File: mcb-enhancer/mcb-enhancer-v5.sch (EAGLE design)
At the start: 127 parts, among them T1 BT138-F, T2 BT138-F, T3 BT138-F, T4 BT138-F, T5 BT138-F, T6 BT138-F, T7 BT138-F, T8 BT138-F

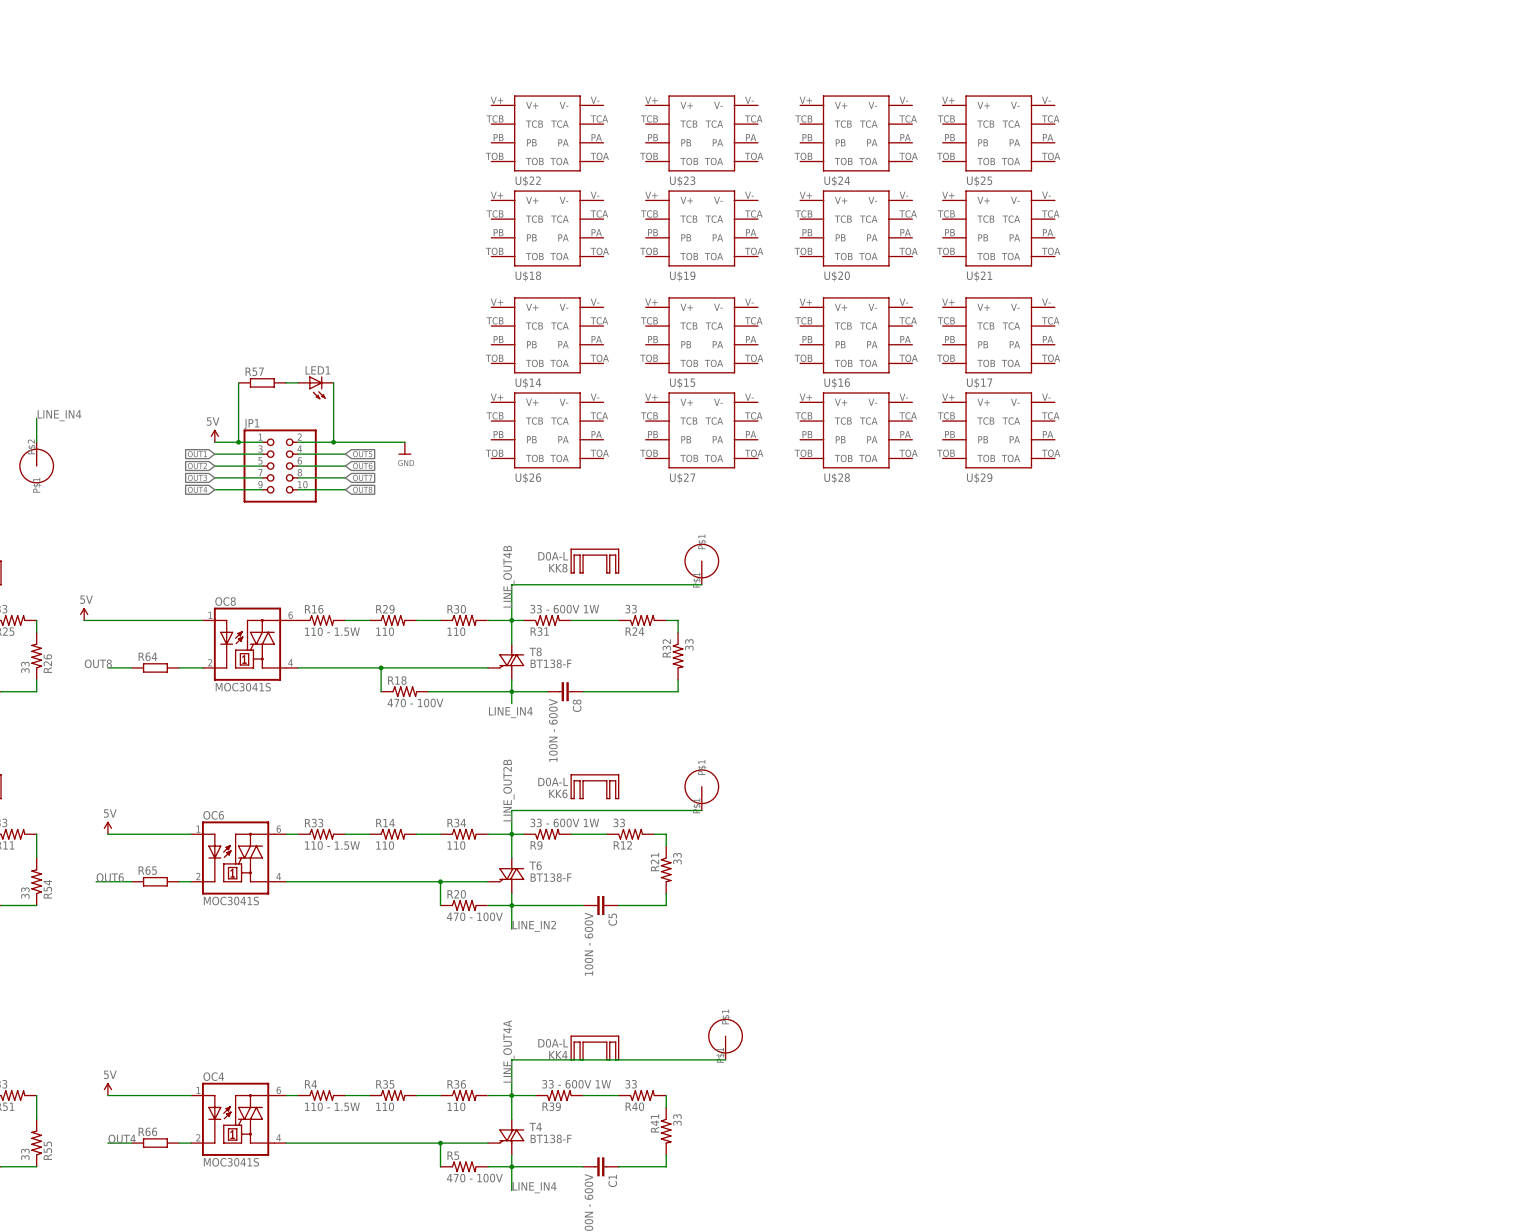
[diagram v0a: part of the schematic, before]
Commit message: add mcb enhancer BoM and gerber
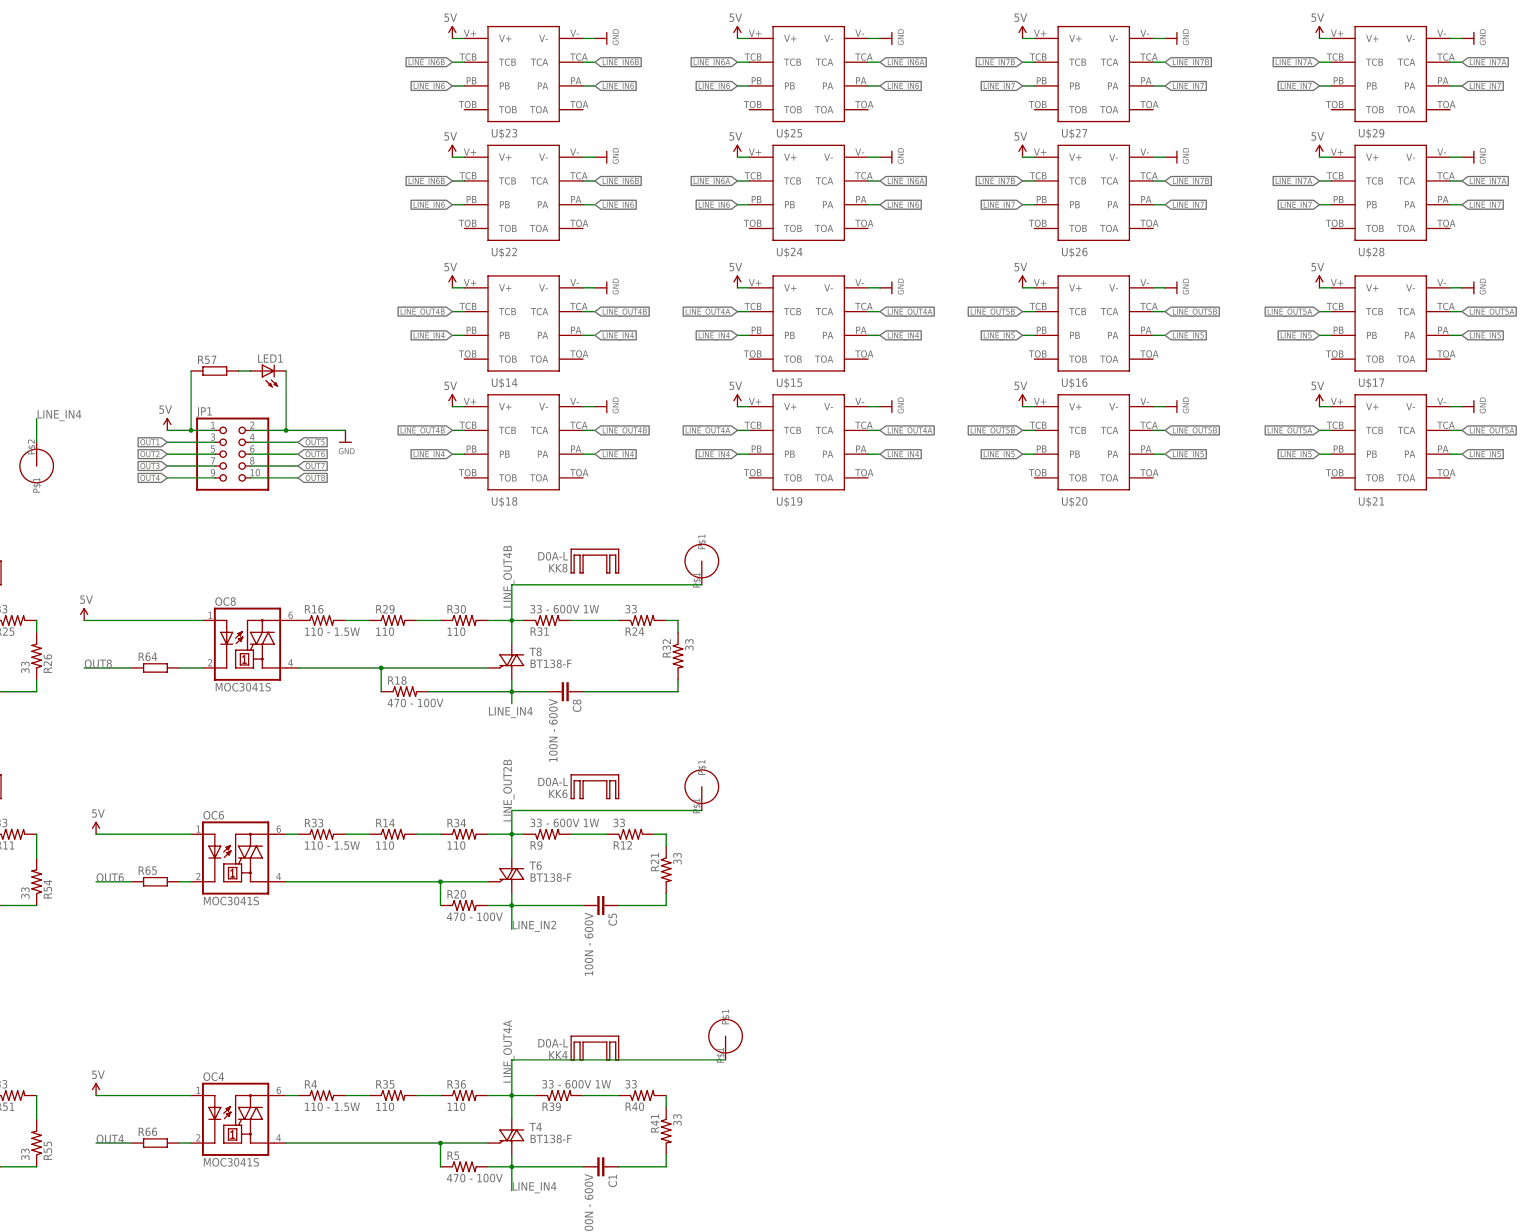
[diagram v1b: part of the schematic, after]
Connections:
- new net LINE_IN5: U$16.PA, U$16.PB, U$17.PA, U$17.PB, U$20.PA, U$20.PB, U$21.PA, U$21.PB
- new net LINE_IN6: U$22.PA, U$22.PB, U$23.PA, U$23.PB, U$24.PA, U$24.PB, U$25.PA, U$25.PB
- new net LINE_IN6A: U$24.TCA, U$24.TCB, U$25.TCA, U$25.TCB
- new net LINE_IN6B: U$22.TCA, U$22.TCB, U$23.TCA, U$23.TCB
- new net LINE_IN7: U$26.PA, U$26.PB, U$27.PA, U$27.PB, U$28.PA, U$28.PB, U$29.PA, U$29.PB
- new net LINE_IN7A: U$28.TCA, U$28.TCB, U$29.TCA, U$29.TCB
- new net LINE_IN7B: U$26.TCA, U$26.TCB, U$27.TCA, U$27.TCB
- new net LINE_OUT5A: U$17.TCA, U$17.TCB, U$21.TCA, U$21.TCB
- new net LINE_OUT5B: U$16.TCA, U$16.TCB, U$20.TCA, U$20.TCB
- net 5V: now also U$14.V+, U$15.V+, U$16.V+, U$17.V+, U$18.V+, U$19.V+, U$20.V+, U$21.V+, U$22.V+, U$23.V+, U$24.V+, U$25.V+, U$26.V+, U$27.V+, U$28.V+, U$29.V+
- net GND: now also U$14.V-, U$15.V-, U$16.V-, U$17.V-, U$18.V-, U$19.V-, U$20.V-, U$21.V-, U$22.V-, U$23.V-, U$24.V-, U$25.V-, U$26.V-, U$27.V-, U$28.V-, U$29.V-
- net LINE_IN4: now also U$14.PA, U$14.PB, U$15.PA, U$15.PB, U$18.PA, U$18.PB, U$19.PA, U$19.PB
- net LINE_OUT4A: now also U$15.TCA, U$15.TCB, U$19.TCA, U$19.TCB
- net LINE_OUT4B: now also U$14.TCA, U$14.TCB, U$18.TCA, U$18.TCB
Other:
- moved on the sheet: JP1, LED1, R57, U$14, U$15, U$16, U$17, U$18, U$19, U$20, U$21, U$22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

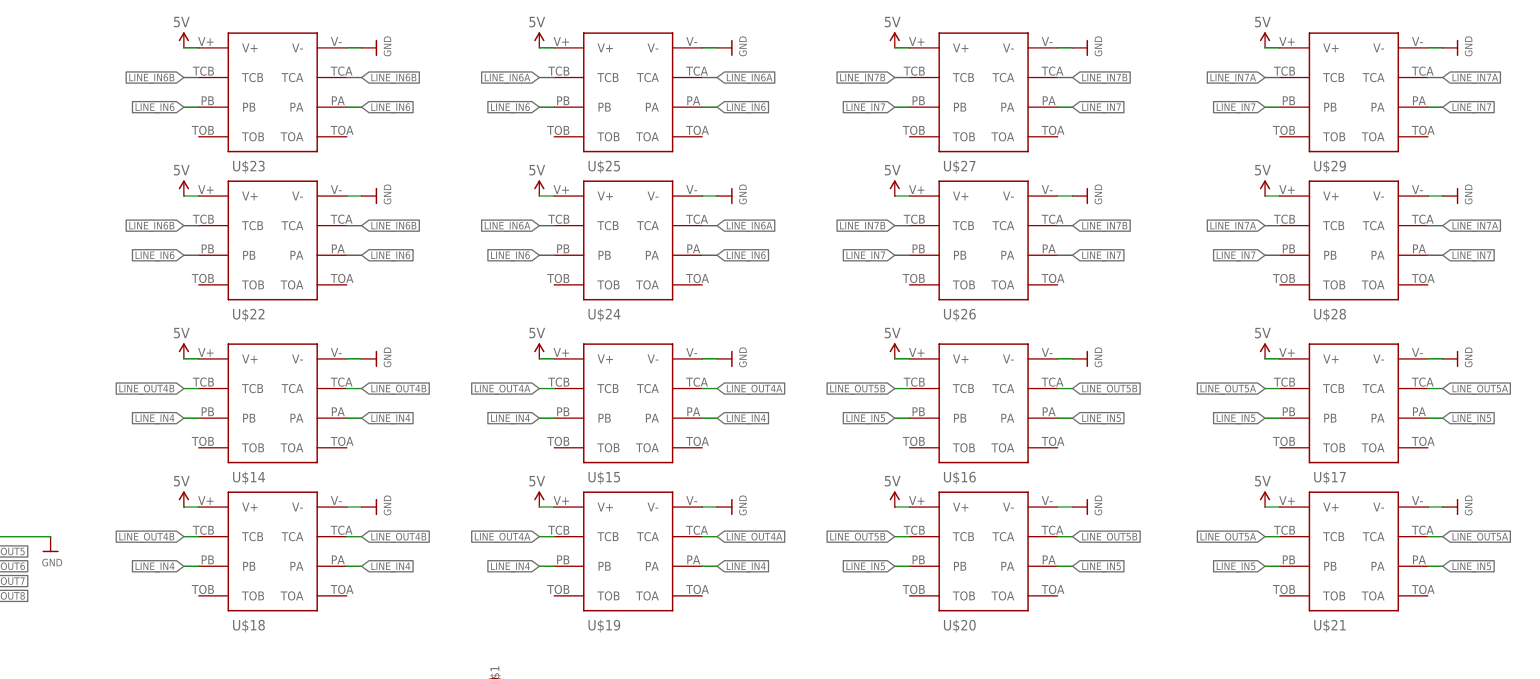
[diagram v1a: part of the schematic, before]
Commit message: routing mcb-enhancer, not DRC/ERC-ed yet
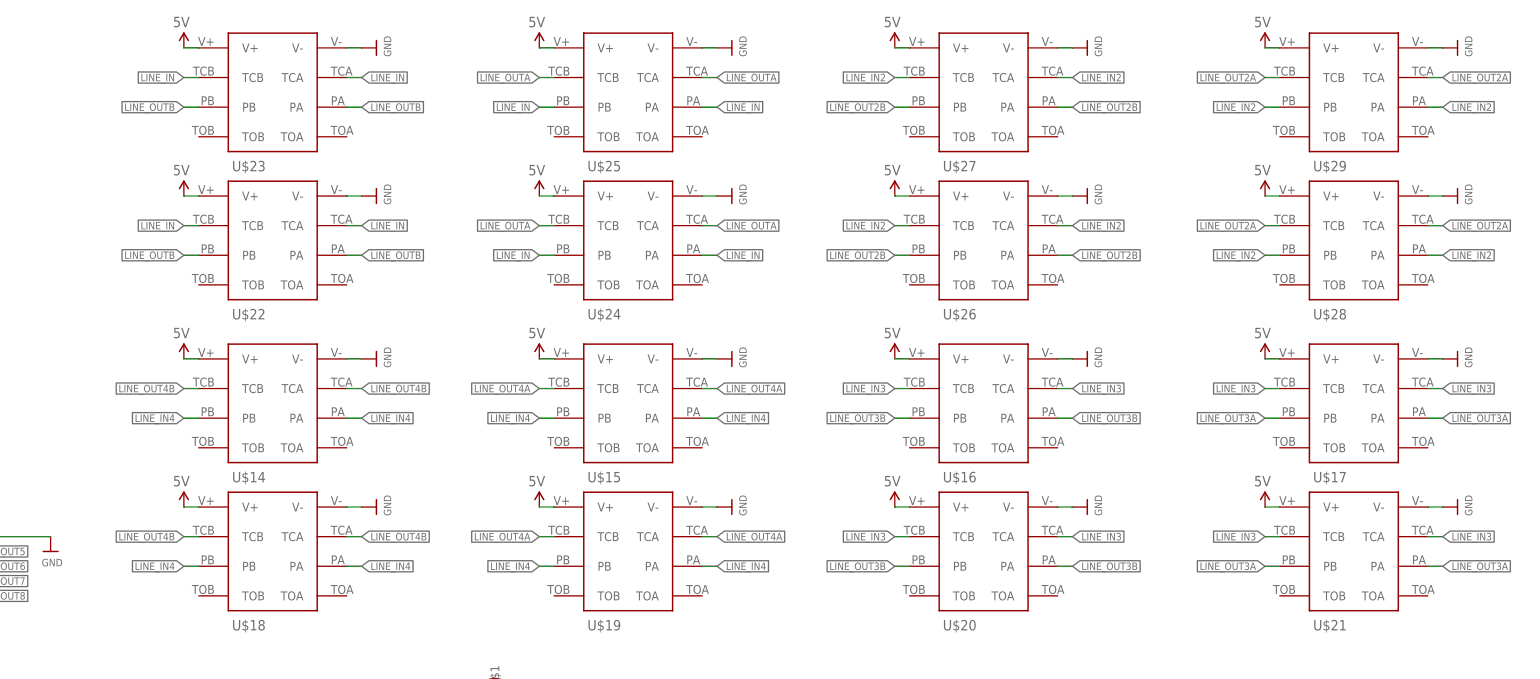
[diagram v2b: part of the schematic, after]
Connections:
- removed net LINE_IN5: U$16.PA, U$16.PB, U$17.PA, U$17.PB, U$20.PA, U$20.PB, U$21.PA, U$21.PB
- removed net LINE_IN6: U$22.PA, U$22.PB, U$23.PA, U$23.PB, U$24.PA, U$24.PB, U$25.PA, U$25.PB
- removed net LINE_IN6A: U$24.TCA, U$24.TCB, U$25.TCA, U$25.TCB
- removed net LINE_IN6B: U$22.TCA, U$22.TCB, U$23.TCA, U$23.TCB
- removed net LINE_IN7: U$26.PA, U$26.PB, U$27.PA, U$27.PB, U$28.PA, U$28.PB, U$29.PA, U$29.PB
- removed net LINE_IN7A: U$28.TCA, U$28.TCB, U$29.TCA, U$29.TCB
- removed net LINE_IN7B: U$26.TCA, U$26.TCB, U$27.TCA, U$27.TCB
- removed net LINE_OUT5A: U$17.TCA, U$17.TCB, U$21.TCA, U$21.TCB
- removed net LINE_OUT5B: U$16.TCA, U$16.TCB, U$20.TCA, U$20.TCB
- net LINE_IN: now also U$22.TCA, U$22.TCB, U$23.TCA, U$23.TCB, U$24.PA, U$24.PB, U$25.PA, U$25.PB
- net LINE_IN2: now also U$26.TCA, U$26.TCB, U$27.TCA, U$27.TCB, U$28.PA, U$28.PB, U$29.PA, U$29.PB
- net LINE_IN3: now also U$16.TCA, U$16.TCB, U$17.TCA, U$17.TCB, U$20.TCA, U$20.TCB, U$21.TCA, U$21.TCB
- net LINE_OUT2A: now also U$28.TCA, U$28.TCB, U$29.TCA, U$29.TCB
- net LINE_OUT2B: now also U$26.PA, U$26.PB, U$27.PA, U$27.PB
- net LINE_OUT3A: now also U$17.PA, U$17.PB, U$21.PA, U$21.PB
- net LINE_OUT3B: now also U$16.PA, U$16.PB, U$20.PA, U$20.PB
- net LINE_OUTA: now also U$24.TCA, U$24.TCB, U$25.TCA, U$25.TCB
- net LINE_OUTB: now also U$22.PA, U$22.PB, U$23.PA, U$23.PB

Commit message: repair silkscreen
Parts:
- LED1: value (none) -> red
- R57: value (none) -> 270
- R60, R61, R62, R63, R64, R65, R66, R67: value (none) -> 200
